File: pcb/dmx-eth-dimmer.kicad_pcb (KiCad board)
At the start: 2 copper layers, 148.6 x 156.2 mm, 118 parts, among them J1 MAINS IN, J10 LOAD, J11 PRG, J12 LOAD, J13 PRG, J14 LOAD, J15 PRG, J16 LOAD, J17 PRG, J18 LOAD, J19 PRG, J20 LOAD, J3 STANDARD ENC28J60, J4 MASTER PROG, J5 PRG, J6 LOAD, J7 PRG, J8 LOAD, J9 PRG, SW1 IP1, SW2 IP2, SW3 IP3, SW4 IP4, SW5 DMXAH, SW6 DMXAL, SW7 SW_DIP_x08, U1 PSU-5VDC, U10 MOC3020M, U11 PIC12(L)F1571/2, U12 MOC3020M, U13 PIC12(L)F1571/2, U14 MOC3020M, U15 PIC12(L)F1571/2, U16 MOC3020M, U17 PIC12(L)F1571/2, U18 MOC3020M, U19 PIC12(L)F1571/2, U20 MOC3020M, U3 74HCT08, U4 4N25, U5 PIC12(L)F1571/2, U6 MOC3020M, U7 PIC12(L)F1571/2, U8 MOC3020M, U9 PIC12(L)F1571/2, Y1 20MHz

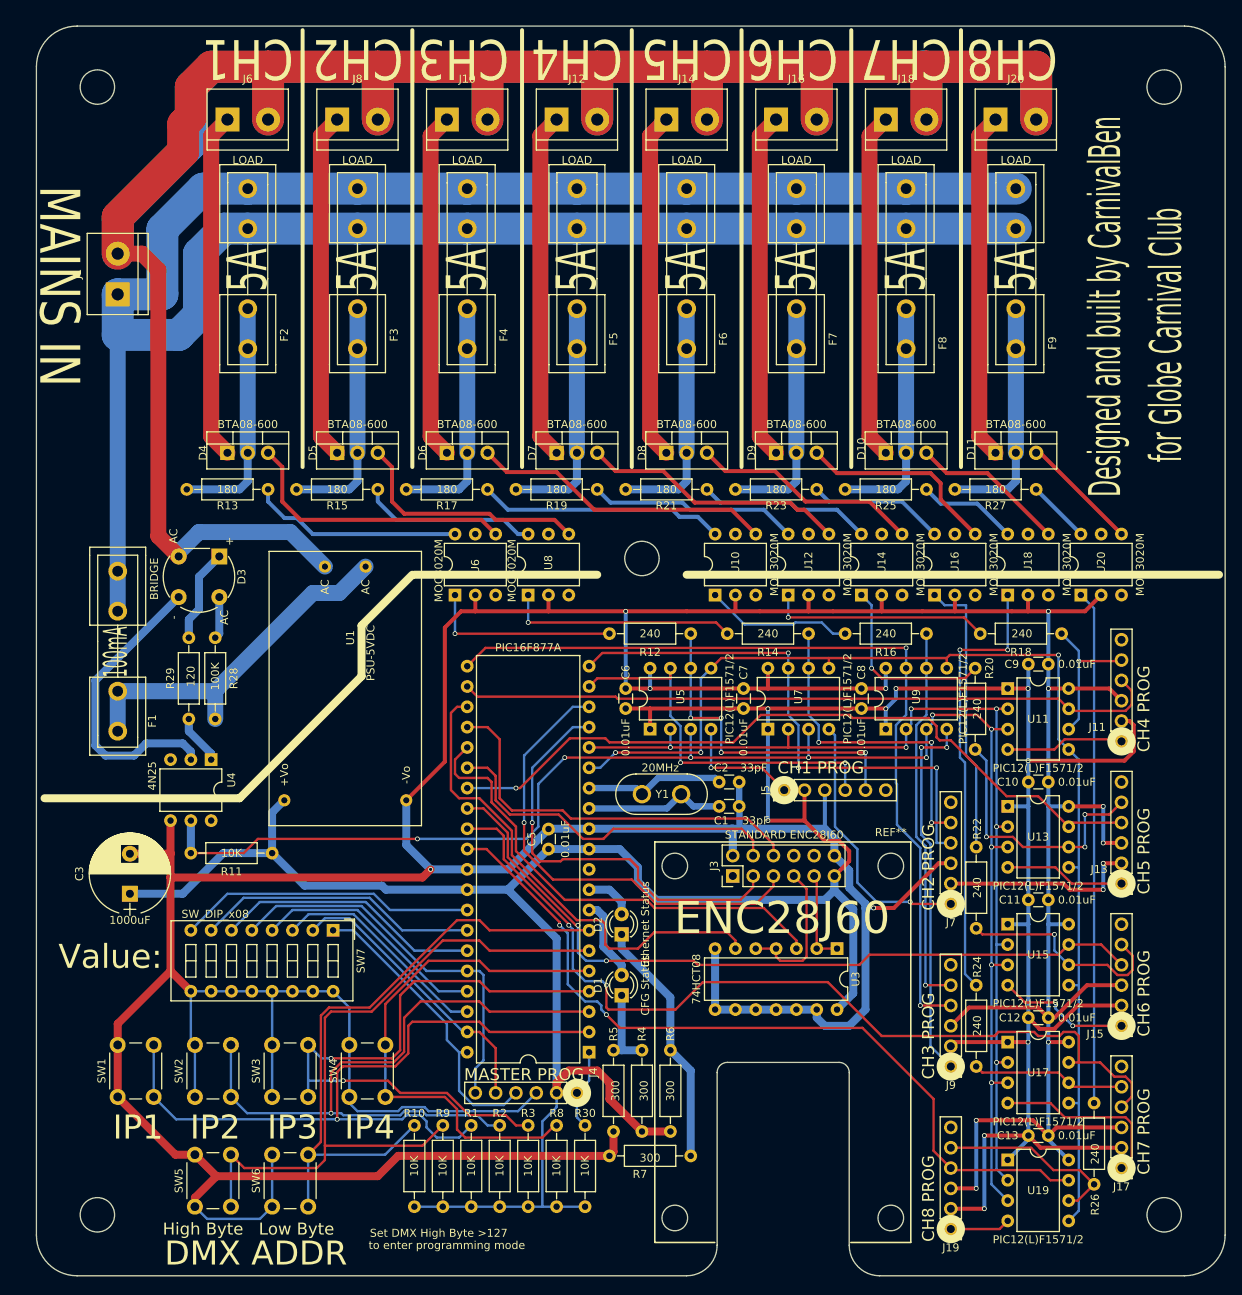
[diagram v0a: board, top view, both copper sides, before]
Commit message: Added Gerbers and watchdog
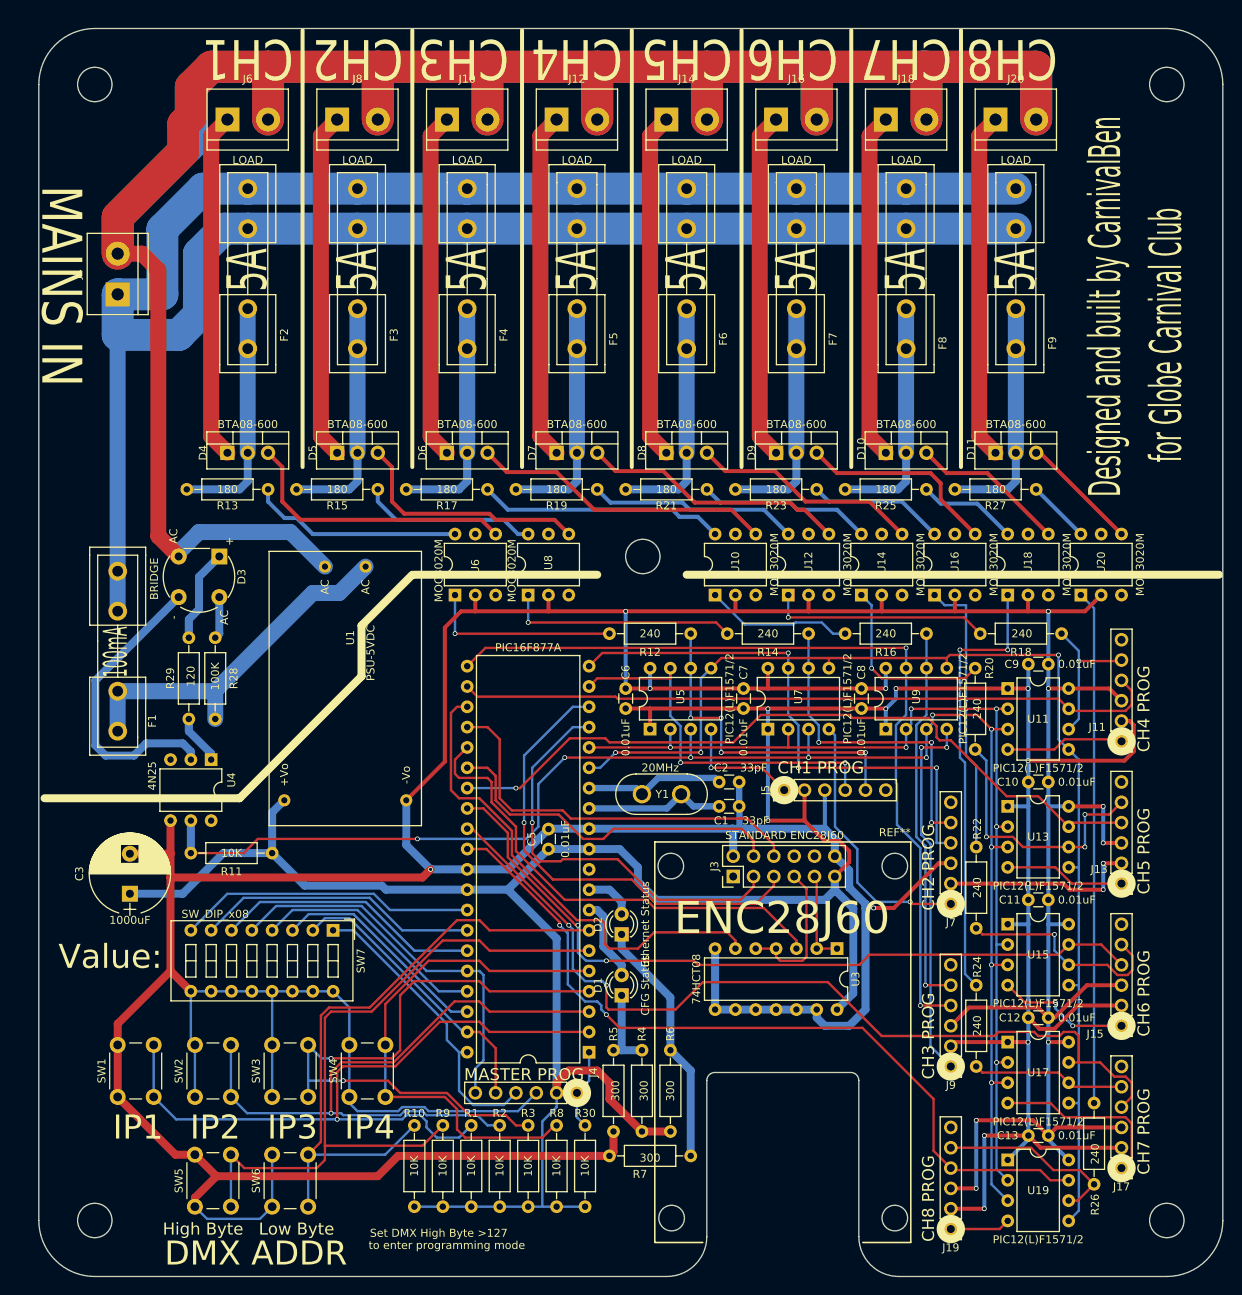
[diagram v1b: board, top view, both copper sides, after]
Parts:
- moved REF** 0.78 mm to (154.0, 162.0)
- moved REF** 0.78 mm to (20.0, 162.0)
- moved REF** 0.50 mm to (92.0, 117.7)
- moved REF** 0.50 mm to (120.0, 117.7)
- moved REF** 0.50 mm to (120.0, 161.7)
- moved REF** 0.46 mm to (154.0, 20.0)
- moved REF** 0.45 mm to (20.0, 20.0)
- moved REF** 0.40 mm to (92.1, 161.7)
- moved REF** 0.27 mm to (88.5, 79.0)
- moved J3 0.08 mm to (99.8, 119.0)
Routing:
- net /IP2: track 86.0 -> 83.5 mm
- net /IP1: track 92.3 -> 90.3 mm
- net /CH7: track 113.0 -> 111.3 mm
- net /RESET: track 53.1 -> 52.1 mm
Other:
- board size 148.6 x 156.2 mm -> 148 x 156 mm
